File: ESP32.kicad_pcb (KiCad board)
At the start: 4 copper layers, 60 parts, among them IC1 CP2102N-A02-GQFN28R, J1 NEMA-5-15P-Male, J2 NEMA-5-15R-Female, J3 10118192-0002LF, J4 0.1" (2.54mm) Headers, K1 G5LE-1, Q1 SS8050, Q2 SS8050, Q3 SS8050, U1 AP2114H-3_3TRG1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

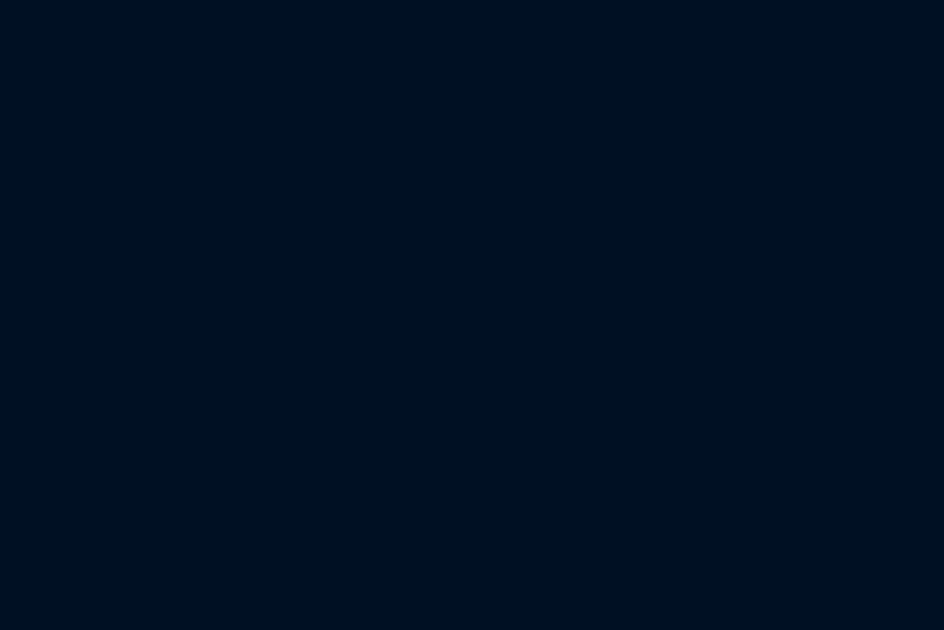
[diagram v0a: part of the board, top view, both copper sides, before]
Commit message: Added solder points for connecting relay outputs to NEMA female Line_Out
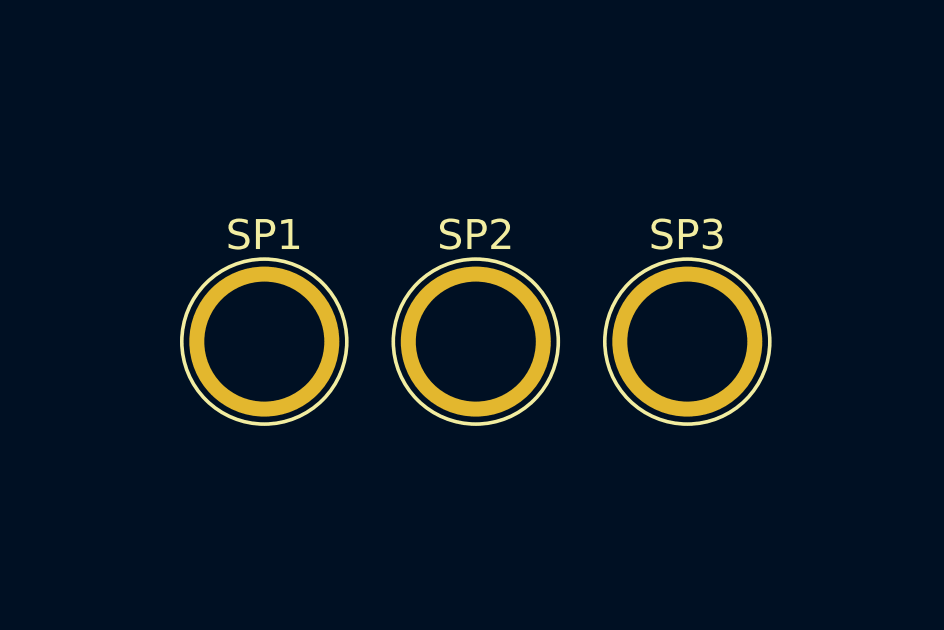
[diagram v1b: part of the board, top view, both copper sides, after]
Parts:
- added SP1: SolderPoint, TestPoint:TestPoint_Plated_Hole_D4.0mm, F.Cu at (436.1, 17.0)
- added SP2: SolderPoint, TestPoint:TestPoint_Plated_Hole_D4.0mm, F.Cu at (443.2, 17.0)
- added SP3: SolderPoint, TestPoint:TestPoint_Plated_Hole_D4.0mm, F.Cu at (450.2, 17.0)
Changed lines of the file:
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@@
-(kicad_pcb (version 20171130) (host pcbnew "(5.1.7)-1")
+(kicad_pcb (version 20171130) (host pcbnew "(5.1.9)-1")
   (general
     (thickness 1.6)
@@
     (tracks 0)
     (zones 0)
-    (modules 60)
+    (modules 63)
     (nets 49)
   )
@@
     (add_net +3V3)
     (add_net AC_GND)
-    (add_net CLK)
-    (add_net CMD)
-    (add_net CTS)
     (add_net D+)
     (add_net D-)
-    (add_net DCD)
-    (add_net DSR)
     (add_net DTR)
     (add_net EN)
@@
     (add_net I2C_SDA)
     (add_net IO0)
-    (add_net IO12)
-    (add_net IO13)
-    (add_net IO14)
-    (add_net IO15)
-    (add_net IO16)
-    (add_net IO17)
     (add_net IO2)
-    (add_net IO25)
-    (add_net IO26)
-    (add_net IO27)
-    (add_net IO32)
-    (add_net IO33)
-    (add_net IO34)
-    (add_net IO35)
     (add_net IO4)
-    (add_net IO5)
     (add_net LINE)
     (add_net LINE_F)
@@
     (add_net "Net-(D5-Pad2)")
     (add_net "Net-(D6-Pad2)")
-    (add_net "Net-(IC1-Pad10)")
     (add_net "Net-(IC1-Pad11)")
-    (add_net "Net-(IC1-Pad12)")
-    (add_net "Net-(IC1-Pad13)")
-    (add_net "Net-(IC1-Pad14)")
-    (add_net "Net-(IC1-Pad15)")
-    (add_net "Net-(IC1-Pad16)")
-    (add_net "Net-(IC1-Pad17)")
-    (add_net "Net-(IC1-Pad20)")
-    (add_net "Net-(IC1-Pad21)")
-    (add_net "Net-(IC1-Pad22)")
     (add_net "Net-(IC1-Pad8)")
     (add_net "Net-(IC1-Pad9)")
@@
     (add_net "Net-(J3-Pad3)")
     (add_net "Net-(JP1-Pad2)")
-    (add_net "Net-(MOD1-Pad32)")
-    (add_net "Net-(PS1-Pad5)")
     (add_net "Net-(Q2-Pad1)")
     (add_net "Net-(Q3-Pad1)")
     (add_net "Net-(R18-Pad2)")
-    (add_net RI)
     (add_net RTS)
     (add_net RXD)
     (add_net RXD0)
-    (add_net SD0)
-    (add_net SD1)
-    (add_net SD2)
-    (add_net SD3)
-    (add_net SENSOR_VN)
-    (add_net SENSOR_VP)
     (add_net SPI_MISO)
     (add_net SPI_MOSI)
@@
     (add_net TXD)
     (add_net TXD0)
-    (add_net USB_ID)
     (add_net VBUS)
   )
+  (module TestPoint:TestPoint_Plated_Hole_D4.0mm (layer F.Cu)
+    (at 450.218 17.018)
+    (descr "Plated Hole as test Point, diameter 4.0mm")
+    (tags "test point plated hole")
+    (attr virtual)
+    (fp_text reference SP3 (at 0 -3.548) (layer F.SilkS)
+      (effects (font (size 1 1) (thickness 0.15)))
+    )
+    (fp_text value SolderPoint (at 0 3.55) (layer F.Fab)
+      (effects (font (size 1 1) (thickness 0.15)))
+    )
+    (fp_circle (center 0 0) (end 0 2.75) (layer F.SilkS) (width 0.12))
+    (fp_circle (center 0 0) (end 3 0) (layer F.CrtYd) (width 0.05))
+    (fp_text user %R (at 0 -3.55) (layer F.Fab)
+      (effects (font (size 1 1) (thickness 0.15)))
+    )
+    (pad 1 thru_hole circle (at 0 0) (size 5 5) (drill 4) (layers *.Cu *.Mask)
+      (net 23 NO))
+  )
+  (module TestPoint:TestPoint_Plated_Hole_D4.0mm (layer F.Cu)
+    (at 443.168 17.018)
+    (descr "Plated Hole as test Point, diameter 4.0mm")
+    (tags "test point plated hole")
+    (attr virtual)
+    (fp_text reference SP2 (at 0 -3.548) (layer F.SilkS)
+      (effects (font (size 1 1) (thickness 0.15)))
+    )
+    (fp_text value SolderPoint (at 0 3.55) (layer F.Fab)
+      (effects (font (size 1 1) (thickness 0.15)))
+    )
+    (fp_circle (center 0 0) (end 0 2.75) (layer F.SilkS) (width 0.12))
+    (fp_circle (center 0 0) (end 3 0) (layer F.CrtYd) (width 0.05))
+    (fp_text user %R (at 0 -3.55) (layer F.Fab)
+      (effects (font (size 1 1) (thickness 0.15)))
+    )
+    (pad 1 thru_hole circle (at 0 0) (size 5 5) (drill 4) (layers *.Cu *.Mask)
+      (net 21 NC))
+  )
+  (module TestPoint:TestPoint_Plated_Hole_D4.0mm (layer F.Cu)
+    (at 436.118 17.018)
+    (descr "Plated Hole as test Point, diameter 4.0mm")
+    (tags "test point plated hole")
+    (attr virtual)
+    (fp_text reference SP1 (at 0 -3.548) (layer F.SilkS)
+      (effects (font (size 1 1) (thickness 0.15)))
+    )
+    (fp_text value SolderPoint (at 0 3.55) (layer F.Fab)
+      (effects (font (size 1 1) (thickness 0.15)))
+    )
+    (fp_circle (center 0 0) (end 0 2.75) (layer F.SilkS) (width 0.12))
+    (fp_circle (center 0 0) (end 3 0) (layer F.CrtYd) (width 0.05))
+    (fp_text user %R (at 0 -3.55) (layer F.Fab)
+      (effects (font (size 1 1) (thickness 0.15)))
+    )
+    (pad 1 thru_hole circle (at 0 0) (size 5 5) (drill 4) (layers *.Cu *.Mask)
+      (net 22 LINE_OUT))
+  )
   (module Resistor_SMD:R_0603_1608Metric_Pad0.98x0.95mm_HandSolder (layer F.Cu)
